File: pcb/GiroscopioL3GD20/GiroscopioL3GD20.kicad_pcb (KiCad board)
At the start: 2 copper layers, 37 x 21 mm, 24 parts, among them J1 Conn_01x09, Q1 BSS138, Q2 BSS138, U1 MIC5225-3.3YM5, U2 L3GD20H

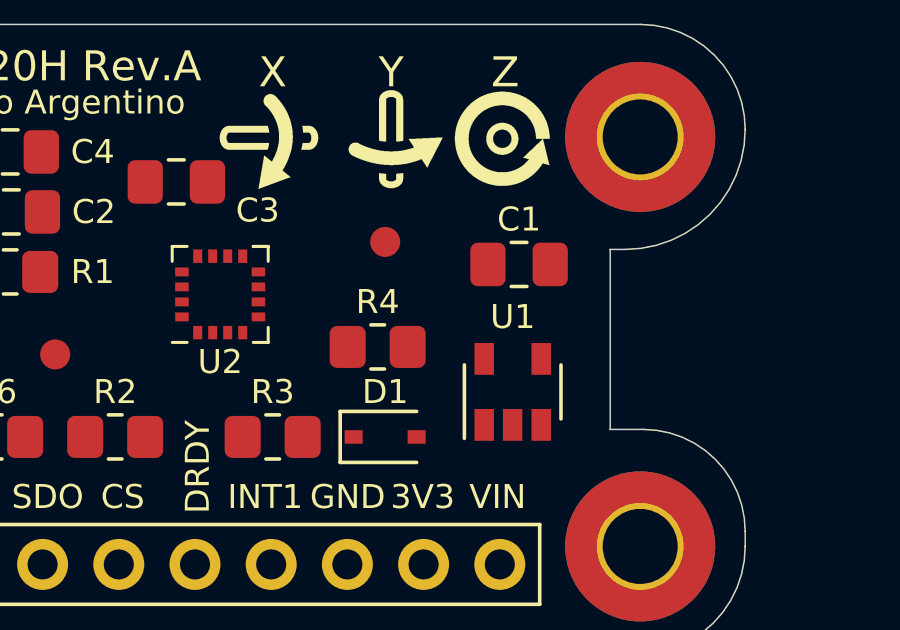
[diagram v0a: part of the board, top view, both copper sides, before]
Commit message: Se agregó info a las notas del PCB
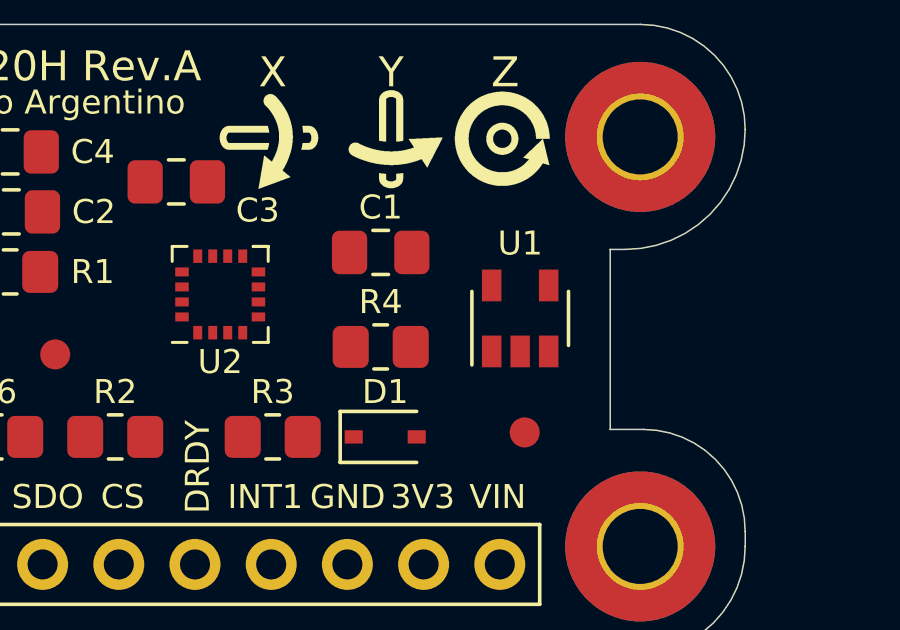
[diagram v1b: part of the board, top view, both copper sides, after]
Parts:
- moved FID1 7.87 mm to (158.6, 108.6)
- moved C1 4.63 mm to (153.8, 102.6)
- moved U1 2.46 mm to (158.4, 104.8)
- moved R4 0.10 mm to (153.8, 105.8)
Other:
- board text added: "(Back copper)"
- board text added: "(Front copper)"
- board text added: "1) Grid size: 0,25 mm, 0,2 mm, 0,1 mm, 0,05 mm."
- board text added: "2) Clearance: 0,2 mm."
- board text added: "3) Vias: 0,8 mm / 0,4 mm - 0,4 mm / 0,2 mm"
- board text added: "4) Tracks: 0,2 mm - 0,4 mm"
- board text added: "5) Finishing surface: HASL"
- board text added: "6) Silkscreen color: White"
- board text added: "7) Manufacturer: Mayer"
- board text added: "Layer 1: 1 Oz"
- board text added: "Layer 2: 1 Oz"
- board text removed: "1 Oz"
- board text removed: "1) Grid size: 0,25 mm, 0,2 mm, 0,1 mm, 0,05 mm"
- board text removed: "2) Clearance: 0,2 mm"
- board text removed: "3) It was required to use 0805 as the minimum acceptable size for all components."
- board text removed: "4) PCB size may be subject to change based after the routing process starts."
- board text removed: "L1 (Top copper)"
- board text removed: "L2 (Bottom copper)"
- board text removed: "Surface finish: HASL Silkscreen color: White"

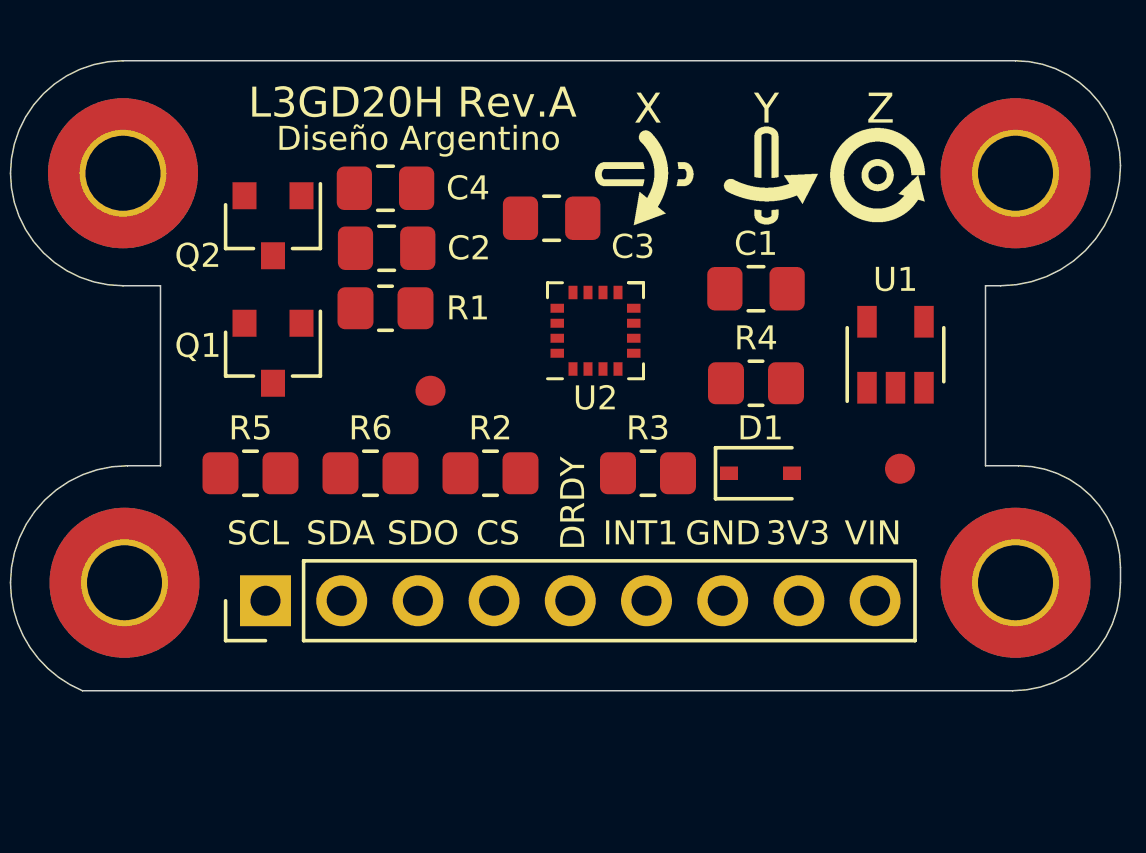
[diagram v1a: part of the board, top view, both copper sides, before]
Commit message: Correcciones del esquematico y ruteo del PCB
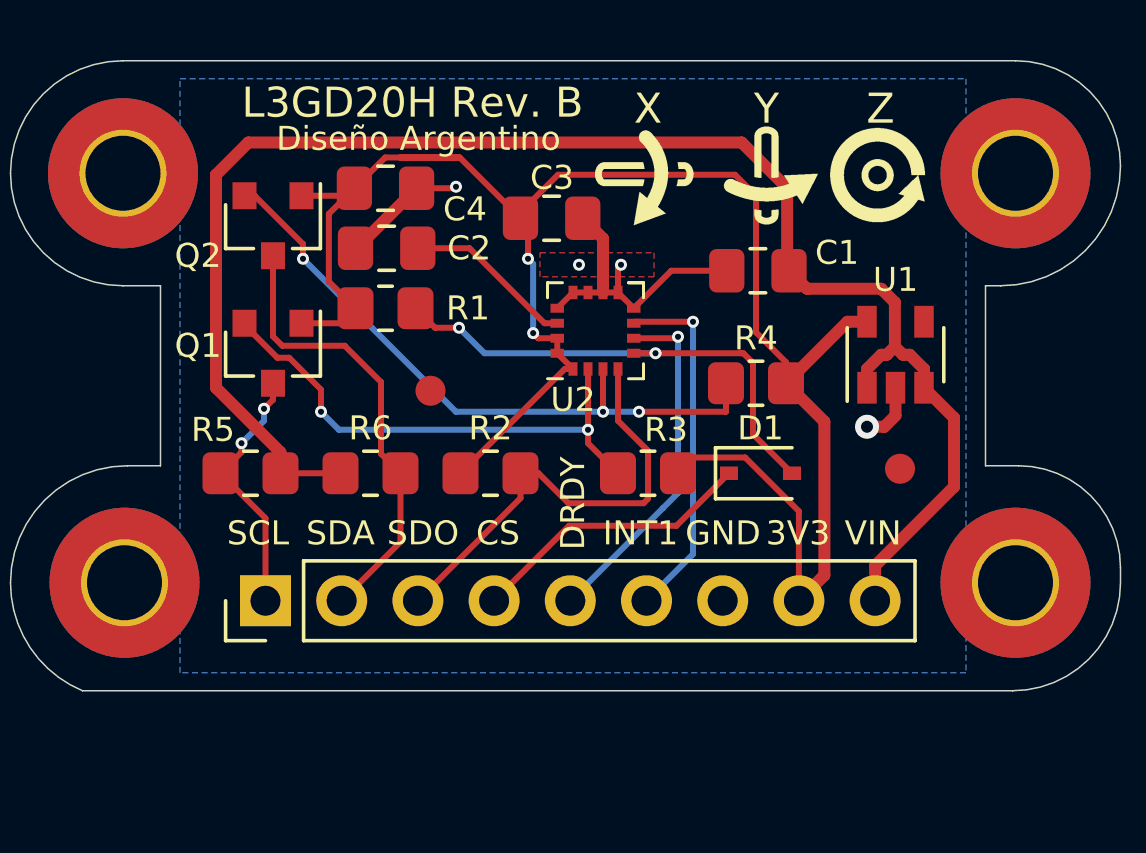
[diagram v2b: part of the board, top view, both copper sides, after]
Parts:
- moved C1 0.60 mm to (153.9, 102.0)
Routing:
- net +3V3: track 0.00 -> 64.4 mm, vias 0 -> 2
- net +5V: track 0.00 -> 56.9 mm
- net /SDA_SDI_SDO_3.3V: track 0.00 -> 21.7 mm, vias 0 -> 3
- net /SCL_SPC_3.3V: track 0.00 -> 17.3 mm, vias 0 -> 2
- net /CS3.3V: track 0.00 -> 17.0 mm, vias 0 -> 2
- net GND: track 0.00 -> 17.0 mm, vias 0 -> 4
- net /SDA_SDI_SDO_5V: track 0.00 -> 15.6 mm
- net /SDO_SAO: track 0.00 -> 15.1 mm
- net /INT1: track 0.00 -> 11.9 mm, vias 0 -> 1
- net /DRDY_INT2: track 0.00 -> 11.8 mm, vias 0 -> 1
- net /CS_5V: track 0.00 -> 9.59 mm
- net /SCL_SPC_5V: track 0.00 -> 8.95 mm, vias 0 -> 2
- net Net-(C2-Pad1): track 0.00 -> 5.69 mm
- added copper zone on B.Cu, net GND
- added copper zone on F.Cu, net GND
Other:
- rule pad_to_mask_clearance: 0.1 -> 0.2
- rule solder_mask_min_width: 0.1 -> 0.2
- rule trace_min: 0.2 -> 0.15
- rule via_min_size: 0.2 -> 0.25
- board text added: "L3GD20H Rev. B"
- board text removed: "L3GD20H Rev.A"

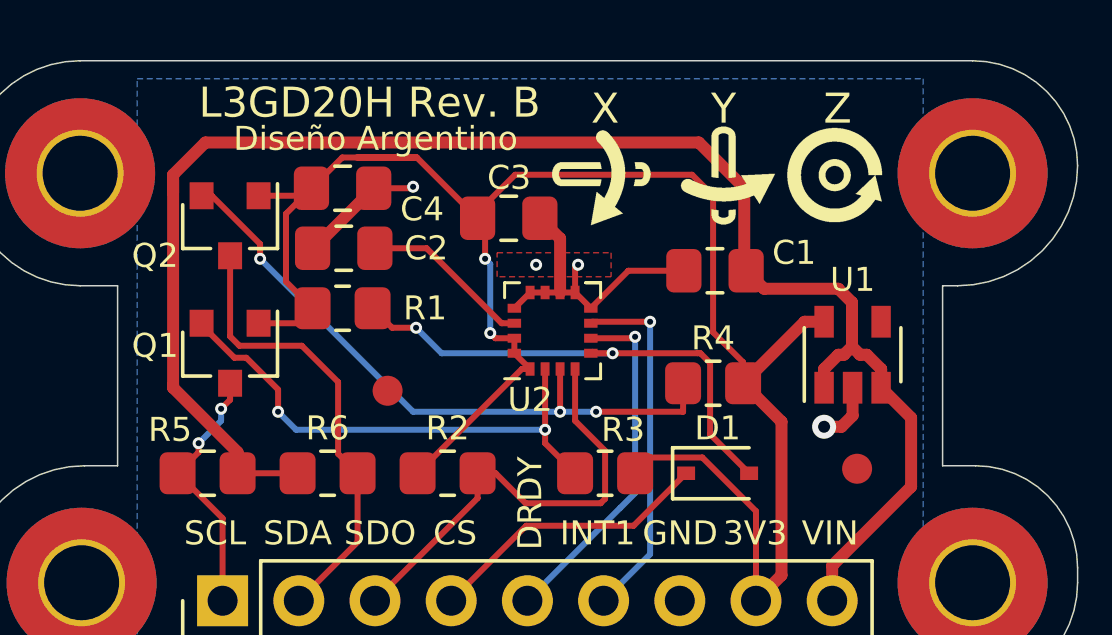
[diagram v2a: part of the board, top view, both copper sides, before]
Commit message: Correcciones. Se agrega Fiducial. Se corrigen posiciones de serigrafias.
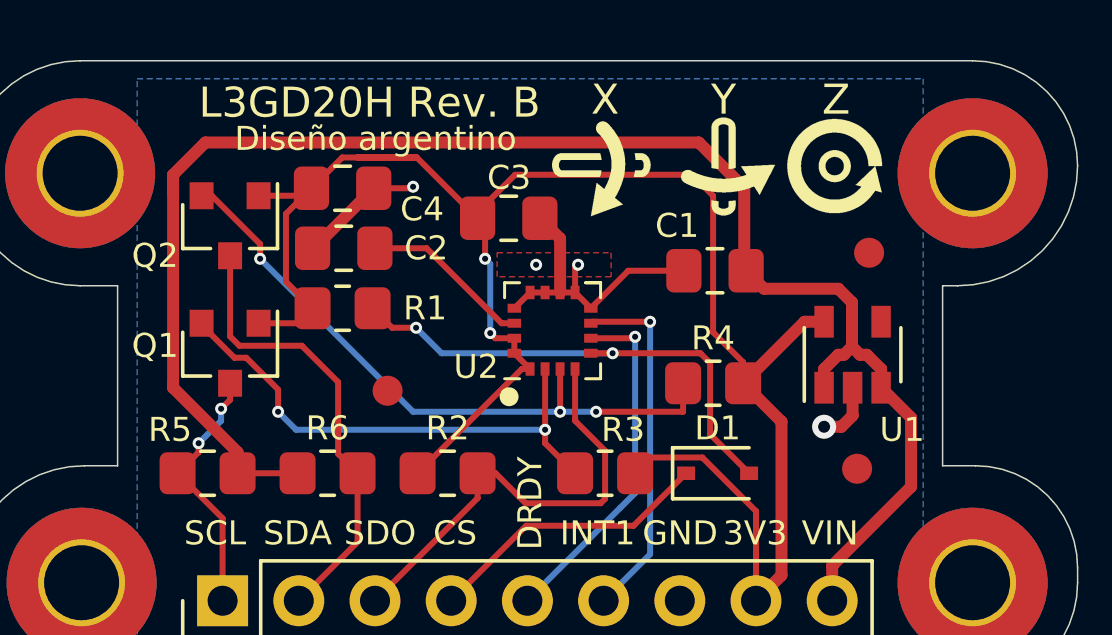
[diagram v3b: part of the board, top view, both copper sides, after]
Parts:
- added FID3: Fiducial, Fiducial:Fiducial_1mm_Mask2mm, F.Cu at (159.0, 101.4)
- moved U$3 0.30 mm to (149.2, 100.2)
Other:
- board text added: "Diseño argentino"
- board text removed: "Diseño Argentino"

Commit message: Mejoras en rotulo y p tierra.
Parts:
- removed REF**: OSHW-Logo_11.4x12mm_Copper, Symbol:OSHW-Logo_11.4x12mm_Copper
